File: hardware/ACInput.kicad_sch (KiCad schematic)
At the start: 8 parts

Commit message: BP2956XS
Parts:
- C202, C203: value 22uF 400v -> 15uF 400v
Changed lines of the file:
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@@
 			)
 		)
-		(property "Value" "22uF 400v"
+		(property "Value" "15uF 400v"
 			(at 163.83 99.4409 0)
 			(effects
@@
 			)
 		)
-		(property "Value" "22uF 400v"
+		(property "Value" "15uF 400v"
 			(at 185.42 99.4409 0)
 			(effects

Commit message: Prototype
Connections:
- net 380V renamed 325V
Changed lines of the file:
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@@
 		)
 	)
-	(hierarchical_label "380V"
+	(hierarchical_label "325V"
 		(shape output)
 		(at 195.58 88.9 0)

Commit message: Tracing draft
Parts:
- removed C203: 15uF 400v, Capacitor_THT:CP_Radial_D13.0mm_P5.00mm, symbol Device:C_Polarized
- removed L201: 1mH 0.5A, Inductor_THT:L_Radial_D10.0mm_P5.00mm_Fastron_07M, symbol Device:L
- C202: value 15uF 400v -> 22uF 400v; footprint Capacitor_THT:CP_Radial_D13.0mm_P5.00mm -> Capacitor_THT:CP_Radial_D10.0mm_P5.00mm
- D201: value MB10M -> MB10S; footprint Package_DIP:DIP-4_W7.62mm -> Package_TO_SOT_SMD:TO-269AA
- R202: footprint Resistor_THT:R_Axial_DIN0309_L9.0mm_D3.2mm_P12.70mm_Horizontal -> Resistor_SMD:R_2512_6332Metric_Pad1.40x3.35mm_HandSolder
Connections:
- net 325V: now also C202.1, D201.3 (+)
- net AC_L: now also C201.2, D201.1, R202.1, RV201.1; no longer R201.1
- net AC_N: now also R201.1; no longer C201.2, D201.1, R202.1, RV201.1

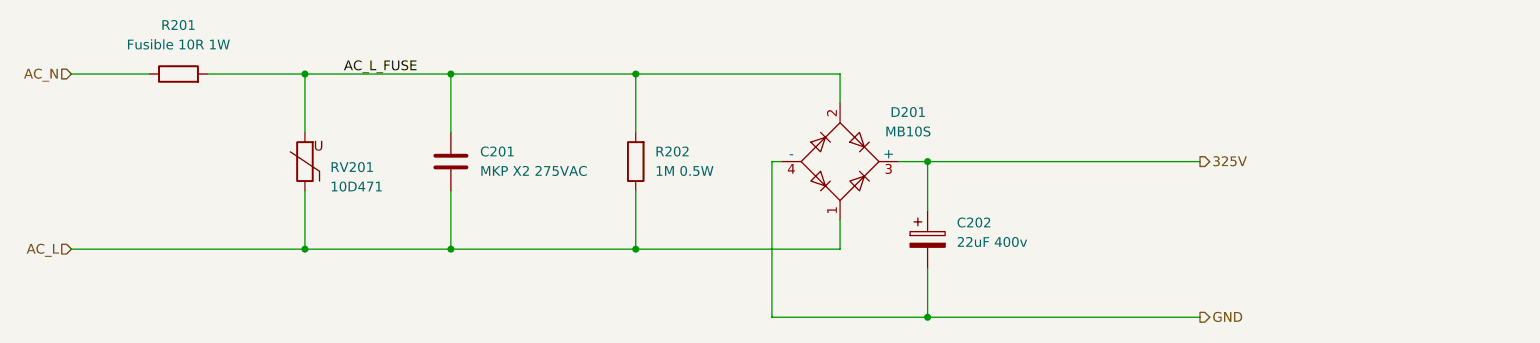
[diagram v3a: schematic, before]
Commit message: Tracing 0.2
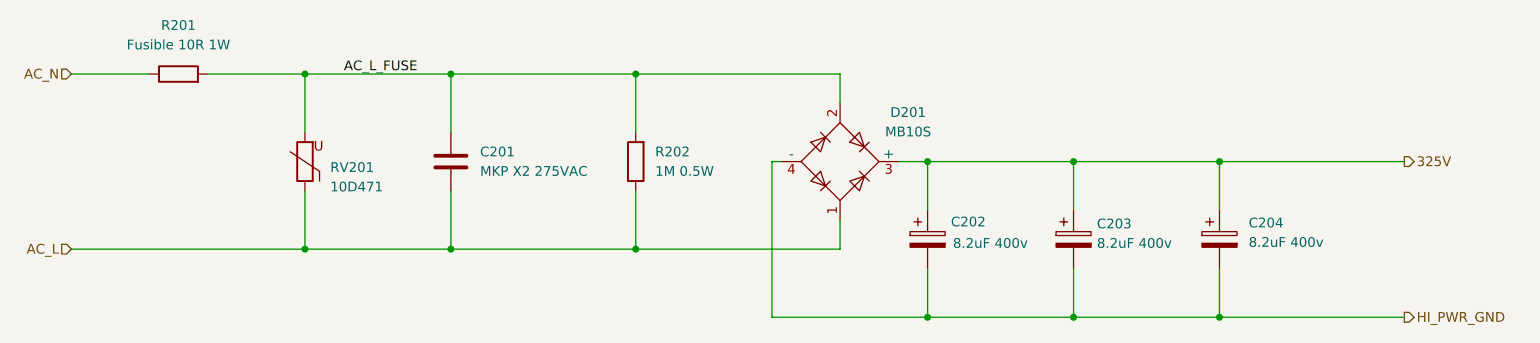
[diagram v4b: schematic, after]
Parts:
- added C203, C204: 8.2uF 400v, Capacitor_THT:CP_Radial_D8.0mm_P3.50mm, symbol Device:C_Polarized
- C202: value 22uF 400v -> 8.2uF 400v; footprint Capacitor_THT:CP_Radial_D10.0mm_P5.00mm -> Capacitor_THT:CP_Radial_D8.0mm_P3.50mm
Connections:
- net 325V: now also C203.1, C204.1
- net GND renamed HI_PWR_GND
- net HI_PWR_GND: now also C203.2, C204.2

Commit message: Use non-hand soldering footprints
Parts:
- R202: footprint Resistor_SMD:R_2512_6332Metric_Pad1.40x3.35mm_HandSolder -> Resistor_SMD:R_2512_6332Metric
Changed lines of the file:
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@@
 			)
 		)
-		(property "Footprint" "Resistor_SMD:R_2512_6332Metric_Pad1.40x3.35mm_HandSolder"
+		(property "Footprint" "Resistor_SMD:R_2512_6332Metric"
 			(at 123.698 88.9 90)
 			(effects
